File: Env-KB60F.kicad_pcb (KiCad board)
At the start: 2 copper layers, 283 x 126.1 mm, 136 parts, among them SW1 EVQ-P7A01P, U1 Pico

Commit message: Mount hole adjustments
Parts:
- removed the G*** at (345.0, 49.0)
- removed the G*** at (317.5, 49.5)
- added H10: MountingHole, MountingHole:MountingHole_2.2mm_M2, F.Cu at (338.0, 155.5)
- added H11: MountingHole, MountingHole:MountingHole_2.1mm, F.Cu at (354.3, 35.7)
- added H8: MountingHole, MountingHole:MountingHole_2.2mm_M2, F.Cu at (99.8, 155.5)
- added H9: MountingHole, MountingHole:MountingHole_2.2mm_M2, F.Cu at (101.8, 84.0)
- moved H3 19.8 mm to (356.8, 138.2)
- moved G*** 11.3 mm to (87.2, 47.5)
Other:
- outline, holes or cut-outs redrawn
- board text added: "USB"
- board text removed: "USB >"

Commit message: Added ANSI Left Shift, Enter and Backslash
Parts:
- removed K_0: KEYSW, MX_Only:MXOnly-1U-NoLED
- added D_28: D, Diode_THT:D_DO-35_SOD27_P7.62mm_Horizontal, F.Cu at (299.0, 51.6)
- added K_1: KEYSW, MX_Only:MXOnly-1U-NoLED, F.Cu at (85.5, 74.5)
- added K_28: KEYSW, MX_Only:MXOnly-1.5U-NoLED, F.Cu at (347.4, 93.5)
- added K_29: KEYSW, MX_Only:MXOnly-2.25U-NoLED, F.Cu at (340.3, 112.6)
- added K_44: KEYSW, MX_Only:MXOnly-2.25U-NoLED, F.Cu at (97.4, 131.7)
- renumbered D_0 to D_1, D_9 to D_10, D_10 to D_11, D_11 to D_12, D_12 to D_13, D_13 to D_14, D_14 to D_15, D_15 to D_16, D_16 to D_17, D_17 to D_18, D_18 to D_19, D_1 to D_2, D_19 to D_20, D_20 to D_21, D_21 to D_22, D_22 to D_23, D_23 to D_24, D_24 to D_25, D_25 to D_26, D_26 to D_27, D_27 to D_29, D_2 to D_3, D_28 to D_30, D_29 to D_31, D_30 to D_32, D_31 to D_33, D_32 to D_34, D_33 to D_35, D_34 to D_36, D_35 to D_37, D_36 to D_38, D_37 to D_39, D_3 to D_4, D_38 to D_40, D_39 to D_41, D_40 to D_42, D_41 to D_43, D_42 to D_44, D_43 to D_45, D_44 to D_46, D_45 to D_47, D_46 to D_48, D_47 to D_49, D_4 to D_5, D_48 to D_50, D_49 to D_51, D_50 to D_52, D_51 to D_53, D_52 to D_54, D_53 to D_55, D_54 to D_56, D_55 to D_57, D_56 to D_58, D_57 to D_59, D_5 to D_6, D_58 to D_60, D_59 to D_61, D_60 to D_62, D_61 to D_63, D_6 to D_7, D_7 to D_8, D_8 to D_9, H6 to H10, H7 to H11, H8 to H2, H2 to H3, H9 to H4, H3 to H5, H10 to H6, H4 to H7, H11 to H8, H5 to H9, K_9 to K_10, K_10 to K_11, K_11 to K_12, K_12 to K_13, K_13 to K_14, K_14 to K_15, K_15 to K_16, K_16 to K_17, K_17 to K_18, K_18 to K_19, K_1 to K_2, K_19 to K_20, K_20 to K_21, K_21 to K_22, K_22 to K_23, K_23 to K_24, K_24 to K_25, K_25 to K_26, K_26 to K_27, K_2 to K_3, K_27 to K_30, K_28 to K_31, K_29 to K_32, K_30 to K_33, K_31 to K_34, K_32 to K_35, K_33 to K_36, K_34 to K_37, K_35 to K_38, K_36 to K_39, K_3 to K_4, K_37 to K_40, K_38 to K_41, K_39 to K_42, K_40 to K_43, K_41 to K_45, K_42 to K_46, K_43 to K_47, K_44 to K_48, K_45 to K_49, K_4 to K_5, K_46 to K_50, K_47 to K_51, K_48 to K_52, K_49 to K_53, K_50 to K_54, K_51 to K_55, K_52 to K_56, K_53 to K_57, K_54 to K_58, K_55 to K_59, K_5 to K_6, K_56 to K_60, K_57 to K_61, K_58 to K_62, K_59 to K_63, K_60 to K_64, K_61 to K_65, K_6 to K_7, K_7 to K_8, K_8 to K_9
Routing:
- net Net-(D_28-Pad2): track 0.00 -> 83.7 mm
- net col14: track 102.6 -> 136.7 mm
- net Net-(D_42-Pad2): track 105.5 -> 122.4 mm
- net col0: track 346.2 -> 356.0 mm
- net Net-(D_43-Pad2): track 96.4 -> 105.9 mm
- net Net-(D_63-Pad2): track 156.5 -> 161.3 mm
- net Net-(D_55-Pad2): track 136.0 -> 138.8 mm
- net Net-(D_62-Pad2): track 158.9 -> 161.7 mm
- net row1: track 235.7 -> 238.2 mm
- net Net-(D_14-Pad2): track 67.9 -> 67.1 mm

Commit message: Designed New Plate, adjusted mount holes and fixed trace issues.
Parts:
- removed H5, H7: MountingHole, MountingHole:MountingHole_2.2mm_M2
- removed H8: MountingHole, MountingHole:MountingHole_2.1mm
- added REF**: KiCad-Logo2_5mm_SilkScreen, Symbol:KiCad-Logo2_5mm_SilkScreen, B.Cu at (347.2, 49.1)
- moved H11 45.1 mm to (350.0, 34.8)
- moved H10 22.1 mm to (314.1, 84.1)
- moved H9 19.5 mm to (218.5, 84.0)
- moved H1 4.27 mm to (218.5, 154.0)
- moved H3 2.15 mm to (87.0, 38.1)
- moved H4 0.11 mm to (101.8, 84.1)
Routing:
- net Net-(D_63-Pad2): track 161.3 -> 154.8 mm
- net col14: track 136.7 -> 142.9 mm
- net Net-(D_41-Pad2): track 108.6 -> 113.1 mm
- net Net-(D_56-Pad2): track 120.5 -> 124.2 mm
- net col0: track 356.0 -> 358.9 mm
- net Net-(D_42-Pad2): track 122.4 -> 124.4 mm
- net Net-(D_62-Pad2): track 161.7 -> 163.0 mm
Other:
- board size 283 x 126.1 mm -> 283 x 126.5 mm

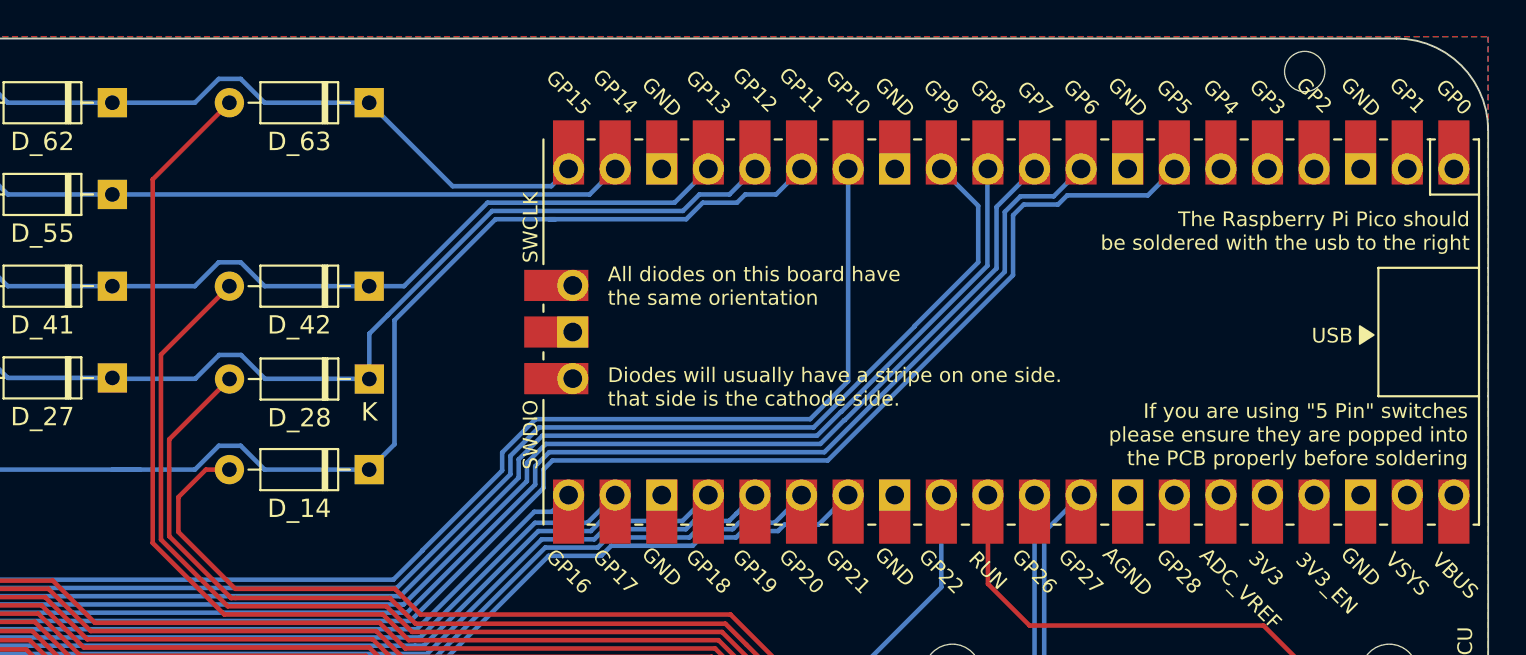
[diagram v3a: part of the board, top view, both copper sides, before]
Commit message: Added a optional top USB port based on feedback
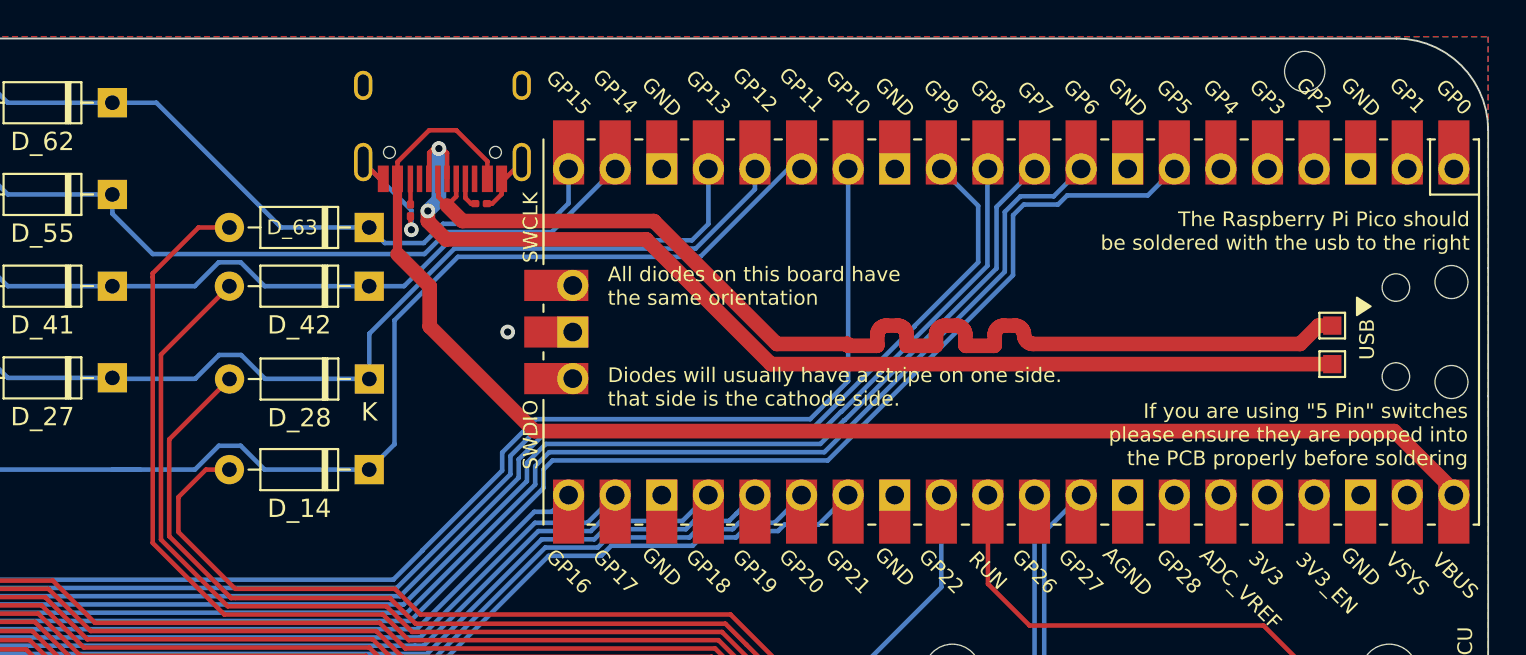
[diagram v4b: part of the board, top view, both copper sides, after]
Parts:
- removed REF**: KiCad-Logo2_5mm_SilkScreen, Symbol:KiCad-Logo2_5mm_SilkScreen
- added 5.1K1: R_Small, Resistor_SMD:R_0201_0603Metric, F.Cu at (305.1, 42.0)
- added 5.1K2: R_Small, Resistor_SMD:R_0201_0603Metric, F.Cu at (301.2, 42.4)
- added J1: TP3 Pad, TestPoint:TestPoint_Pad_1.0x1.0mm, F.Cu at (351.5, 48.6)
- added J2: TP2 Pad, TestPoint:TestPoint_Pad_1.0x1.0mm, F.Cu at (351.5, 50.8)
- added USB1: HRO-TYPE-C-31-M-12, HRO-TYPE-C31-M-12:HRO-TYPE-C-31-M-12, F.Cu at (303.0, 33.0)
- moved D_63 6.80 mm to (299.0, 43.3)
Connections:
- U1 pad 40: Net-(U1-Pad40) -> VBUS
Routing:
- net VBUS: track 0.00 -> 76.7 mm
- net USB2_P: track 0.00 -> 61.3 mm, vias 0 -> 2
- net USB2_N: track 0.00 -> 60.1 mm
- net GND: track 0.28 -> 10.6 mm, vias 0 -> 2
- net Net-(D_63-Pad2): track 154.8 -> 149.0 mm
- net row3: track 222.9 -> 226.2 mm
- net row4: track 220.7 -> 223.3 mm
- net row2: track 231.6 -> 233.4 mm
- net Net-(5.1K1-Pad1): track 0.00 -> 1.71 mm
- net Net-(5.1K2-Pad2): track 0.00 -> 1.40 mm
- net row1: track 238.2 -> 238.9 mm
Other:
- net class USB* added: clearance 0.2, trace_width 0.8, via_dia 0.8, via_drill 0.4

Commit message: Added missing graphic
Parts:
- added G***: LOGO, AKLogo:diode, F.Cu at (317.0, 49.4)
